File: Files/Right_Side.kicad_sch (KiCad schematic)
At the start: 77 parts, among them J4 USB_C_Receptacle, J5 Conn_01x03_Pin, J6 USB_C_Receptacle, U5 W25Q128JVS, U6 XC6206-3.3_SOT, U7 USBLC6-2SC6, U8 RP2040, Y2 Crystal_GND24

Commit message: placed companets and semi routed
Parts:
- C19, C20, C21, C22, C23, C24, C25, C27, C28, C29, C31, C32, C33, C34, C35, C36: footprint ScottoKeebs_Components:Capacitor_0603 -> Capacitor_SMD:C_0805_2012Metric_Pad1.18x1.45mm_HandSolder
- C26, C30: footprint ScottoKeebs_Components:Capacitor_0402 -> Capacitor_SMD:C_0805_2012Metric_Pad1.18x1.45mm_HandSolder
- R11, R12, R13, R14, R15, R16, R17, R18, R19, R20: footprint Resistor_SMD:R_0603_1608Metric -> Resistor_SMD:R_0805_2012Metric_Pad1.20x1.40mm_HandSolder
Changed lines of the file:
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@@
 			)
 		)
-		(property "Footprint" "ScottoKeebs_Components:Capacitor_0603"
+		(property "Footprint" "Capacitor_SMD:C_0805_2012Metric_Pad1.18x1.45mm_HandSolder"
 			(at 152.4 134.3152 0)
 			(effects
@@
 			)
 		)
-		(property "Footprint" "ScottoKeebs_Components:Capacitor_0402"
+		(property "Footprint" "Capacitor_SMD:C_0805_2012Metric_Pad1.18x1.45mm_HandSolder"
 			(at 191.4652 77.47 0)
 			(effects
@@
 			)
 		)
-		(property "Footprint" "ScottoKeebs_Components:Capacitor_0603"
+		(property "Footprint" "Capacitor_SMD:C_0805_2012Metric_Pad1.18x1.45mm_HandSolder"
 			(at 260.0452 62.23 0)
 			(effects
@@
 			)
 		)
-		(property "Footprint" "ScottoKeebs_Components:Capacitor_0603"
+		(property "Footprint" "Capacitor_SMD:C_0805_2012Metric_Pad1.18x1.45mm_HandSolder"
 			(at 118.11 108.2548 0)
 			(effects
@@
 			)
 		)
-		(property "Footprint" "ScottoKeebs_Components:Capacitor_0603"
+		(property "Footprint" "Capacitor_SMD:C_0805_2012Metric_Pad1.18x1.45mm_HandSolder"
 			(at 152.4 144.4752 0)
 			(effects
@@
 			)
 		)
-		(property "Footprint" "Resistor_SMD:R_0603_1608Metric"
+		(property "Footprint" "Resistor_SMD:R_0805_2012Metric_Pad1.20x1.40mm_HandSolder"
 			(at 190.5 96.012 90)
 			(effects
@@
 			)
 		)
-		(property "Footprint" "Resistor_SMD:R_0603_1608Metric"
+		(property "Footprint" "Resistor_SMD:R_0805_2012Metric_Pad1.20x1.40mm_HandSolder"
 			(at 92.71 187.198 90)
 			(effects
@@
 			)
 		)
-		(property "Footprint" "Resistor_SMD:R_0603_1608Metric"
+		(property "Footprint" "Resistor_SMD:R_0805_2012Metric_Pad1.20x1.40mm_HandSolder"
 			(at 216.662 209.55 90)
 			(effects
@@
 			)
 		)
-		(property "Footprint" "Resistor_SMD:R_0603_1608Metric"
+		(property "Footprint" "Resistor_SMD:R_0805_2012Metric_Pad1.20x1.40mm_HandSolder"
 			(at 186.69 145.288 90)
 			(effects
@@
 			)
 		)
-		(property "Footprint" "Resistor_SMD:R_0603_1608Metric"
+		(property "Footprint" "Resistor_SMD:R_0805_2012Metric_Pad1.20x1.40mm_HandSolder"
 			(at 81.28 116.078 90)
 			(effects
@@
 			)
 		)
-		(property "Footprint" "Resistor_SMD:R_0603_1608Metric"
+		(property "Footprint" "Resistor_SMD:R_0805_2012Metric_Pad1.20x1.40mm_HandSolder"
 			(at 92.71 189.738 90)
 			(effects
@@
 			)
 		)
-		(property "Footprint" "ScottoKeebs_Components:Capacitor_0603"
+		(property "Footprint" "Capacitor_SMD:C_0805_2012Metric_Pad1.18x1.45mm_HandSolder"
 			(at 246.0752 43.18 0)
 			(effects
@@
 			)
 		)
-		(property "Footprint" "ScottoKeebs_Components:Capacitor_0603"
+		(property "Footprint" "Capacitor_SMD:C_0805_2012Metric_Pad1.18x1.45mm_HandSolder"
 			(at 191.4652 62.23 0)
 			(effects
@@
 			)
 		)
-		(property "Footprint" "ScottoKeebs_Components:Capacitor_0603"
+		(property "Footprint" "Capacitor_SMD:C_0805_2012Metric_Pad1.18x1.45mm_HandSolder"
 			(at 296.8752 62.23 0)
 			(effects
@@
 			)
 		)
-		(property "Footprint" "Resistor_SMD:R_0603_1608Metric"
+		(property "Footprint" "Resistor_SMD:R_0805_2012Metric_Pad1.20x1.40mm_HandSolder"
 			(at 186.182 209.55 90)
 			(effects
@@
 			)
 		)
-		(property "Footprint" "ScottoKeebs_Components:Capacitor_0603"
+		(property "Footprint" "Capacitor_SMD:C_0805_2012Metric_Pad1.18x1.45mm_HandSolder"
 			(at 323.5452 62.23 0)
 			(effects
@@
 			)
 		)
-		(property "Footprint" "ScottoKeebs_Components:Capacitor_0603"
+		(property "Footprint" "Capacitor_SMD:C_0805_2012Metric_Pad1.18x1.45mm_HandSolder"
 			(at 284.1752 62.23 0)
 			(effects
@@
 			)
 		)
-		(property "Footprint" "ScottoKeebs_Components:Capacitor_0603"
+		(property "Footprint" "Capacitor_SMD:C_0805_2012Metric_Pad1.18x1.45mm_HandSolder"
 			(at 110.1852 187.96 0)
 			(effects
@@
 			)
 		)
-		(property "Footprint" "Resistor_SMD:R_0603_1608Metric"
+		(property "Footprint" "Resistor_SMD:R_0805_2012Metric_Pad1.20x1.40mm_HandSolder"
 			(at 190.5 97.028 90)
 			(effects
@@
 			)
 		)
-		(property "Footprint" "ScottoKeebs_Components:Capacitor_0603"
+		(property "Footprint" "Capacitor_SMD:C_0805_2012Metric_Pad1.18x1.45mm_HandSolder"
 			(at 247.3452 62.23 0)
 			(effects
@@
 			)
 		)
-		(property "Footprint" "ScottoKeebs_Components:Capacitor_0603"
+		(property "Footprint" "Capacitor_SMD:C_0805_2012Metric_Pad1.18x1.45mm_HandSolder"
 			(at 202.8952 62.23 0)
 			(effects
@@
 			)
 		)
-		(property "Footprint" "ScottoKeebs_Components:Capacitor_0603"
+		(property "Footprint" "Capacitor_SMD:C_0805_2012Metric_Pad1.18x1.45mm_HandSolder"
 			(at 89.2048 58.42 0)
 			(effects
@@
 			)
 		)
-		(property "Footprint" "ScottoKeebs_Components:Capacitor_0603"
+		(property "Footprint" "Capacitor_SMD:C_0805_2012Metric_Pad1.18x1.45mm_HandSolder"
 			(at 272.7452 62.23 0)
 			(effects
@@
 			)
 		)
-		(property "Footprint" "Resistor_SMD:R_0603_1608Metric"
+		(property "Footprint" "Resistor_SMD:R_0805_2012Metric_Pad1.20x1.40mm_HandSolder"
 			(at 82.042 52.07 90)
 			(effects
@@
 			)
 		)
-		(property "Footprint" "ScottoKeebs_Components:Capacitor_0402"
+		(property "Footprint" "Capacitor_SMD:C_0805_2012Metric_Pad1.18x1.45mm_HandSolder"
 			(at 247.3452 77.47 0)
 			(effects
@@
 			)
 		)
-		(property "Footprint" "Resistor_SMD:R_0603_1608Metric"
+		(property "Footprint" "Resistor_SMD:R_0805_2012Metric_Pad1.20x1.40mm_HandSolder"
 			(at 91.948 113.03 90)
 			(effects
@@
 			)
 		)
-		(property "Footprint" "ScottoKeebs_Components:Capacitor_0603"
+		(property "Footprint" "Capacitor_SMD:C_0805_2012Metric_Pad1.18x1.45mm_HandSolder"
 			(at 309.5752 62.23 0)
 			(effects
@@
 			)
 		)
-		(property "Footprint" "ScottoKeebs_Components:Capacitor_0603"
+		(property "Footprint" "Capacitor_SMD:C_0805_2012Metric_Pad1.18x1.45mm_HandSolder"
 			(at 143.2052 187.96 0)
 			(effects

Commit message: added 5v pads
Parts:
- C19, C20, C21, C22, C23, C24, C25, C26, C27, C28, C29, C30, C31, C32, C33, C34, C35, C36: footprint Capacitor_SMD:C_0805_2012Metric_Pad1.18x1.45mm_HandSolder -> Capacitor_SMD:C_0805_2012Metric
- R11, R12, R13, R14, R15, R16, R17, R18, R19, R20: footprint Resistor_SMD:R_0805_2012Metric_Pad1.20x1.40mm_HandSolder -> Resistor_SMD:R_0805_2012Metric
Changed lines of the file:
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@@
 			)
 		)
-		(property "Footprint" "Capacitor_SMD:C_0805_2012Metric_Pad1.18x1.45mm_HandSolder"
+		(property "Footprint" "Capacitor_SMD:C_0805_2012Metric"
 			(at 152.4 134.3152 0)
 			(effects
@@
 			)
 		)
-		(property "Footprint" "Capacitor_SMD:C_0805_2012Metric_Pad1.18x1.45mm_HandSolder"
+		(property "Footprint" "Capacitor_SMD:C_0805_2012Metric"
 			(at 191.4652 77.47 0)
 			(effects
@@
 			)
 		)
-		(property "Footprint" "Capacitor_SMD:C_0805_2012Metric_Pad1.18x1.45mm_HandSolder"
+		(property "Footprint" "Capacitor_SMD:C_0805_2012Metric"
 			(at 260.0452 62.23 0)
 			(effects
@@
 			)
 		)
-		(property "Footprint" "Capacitor_SMD:C_0805_2012Metric_Pad1.18x1.45mm_HandSolder"
+		(property "Footprint" "Capacitor_SMD:C_0805_2012Metric"
 			(at 118.11 108.2548 0)
 			(effects
@@
 			)
 		)
-		(property "Footprint" "Capacitor_SMD:C_0805_2012Metric_Pad1.18x1.45mm_HandSolder"
+		(property "Footprint" "Capacitor_SMD:C_0805_2012Metric"
 			(at 152.4 144.4752 0)
 			(effects
@@
 			)
 		)
-		(property "Footprint" "Resistor_SMD:R_0805_2012Metric_Pad1.20x1.40mm_HandSolder"
+		(property "Footprint" "Resistor_SMD:R_0805_2012Metric"
 			(at 190.5 96.012 90)
 			(effects
@@
 			)
 		)
-		(property "Footprint" "Resistor_SMD:R_0805_2012Metric_Pad1.20x1.40mm_HandSolder"
+		(property "Footprint" "Resistor_SMD:R_0805_2012Metric"
 			(at 92.71 187.198 90)
 			(effects
@@
 			)
 		)
-		(property "Footprint" "Resistor_SMD:R_0805_2012Metric_Pad1.20x1.40mm_HandSolder"
+		(property "Footprint" "Resistor_SMD:R_0805_2012Metric"
 			(at 216.662 209.55 90)
 			(effects
@@
 			)
 		)
-		(property "Footprint" "Resistor_SMD:R_0805_2012Metric_Pad1.20x1.40mm_HandSolder"
+		(property "Footprint" "Resistor_SMD:R_0805_2012Metric"
 			(at 186.69 145.288 90)
 			(effects
@@
 			)
 		)
-		(property "Footprint" "Resistor_SMD:R_0805_2012Metric_Pad1.20x1.40mm_HandSolder"
+		(property "Footprint" "Resistor_SMD:R_0805_2012Metric"
 			(at 81.28 116.078 90)
 			(effects
@@
 			)
 		)
-		(property "Footprint" "Resistor_SMD:R_0805_2012Metric_Pad1.20x1.40mm_HandSolder"
+		(property "Footprint" "Resistor_SMD:R_0805_2012Metric"
 			(at 92.71 189.738 90)
 			(effects
@@
 			)
 		)
-		(property "Footprint" "Capacitor_SMD:C_0805_2012Metric_Pad1.18x1.45mm_HandSolder"
+		(property "Footprint" "Capacitor_SMD:C_0805_2012Metric"
 			(at 246.0752 43.18 0)
 			(effects
@@
 			)
 		)
-		(property "Footprint" "Capacitor_SMD:C_0805_2012Metric_Pad1.18x1.45mm_HandSolder"
+		(property "Footprint" "Capacitor_SMD:C_0805_2012Metric"
 			(at 191.4652 62.23 0)
 			(effects
@@
 			)
 		)
-		(property "Footprint" "Capacitor_SMD:C_0805_2012Metric_Pad1.18x1.45mm_HandSolder"
+		(property "Footprint" "Capacitor_SMD:C_0805_2012Metric"
 			(at 296.8752 62.23 0)
 			(effects
@@
 			)
 		)
-		(property "Footprint" "Resistor_SMD:R_0805_2012Metric_Pad1.20x1.40mm_HandSolder"
+		(property "Footprint" "Resistor_SMD:R_0805_2012Metric"
 			(at 186.182 209.55 90)
 			(effects
@@
 			)
 		)
-		(property "Footprint" "Capacitor_SMD:C_0805_2012Metric_Pad1.18x1.45mm_HandSolder"
+		(property "Footprint" "Capacitor_SMD:C_0805_2012Metric"
 			(at 323.5452 62.23 0)
 			(effects
@@
 			)
 		)
-		(property "Footprint" "Capacitor_SMD:C_0805_2012Metric_Pad1.18x1.45mm_HandSolder"
+		(property "Footprint" "Capacitor_SMD:C_0805_2012Metric"
 			(at 284.1752 62.23 0)
 			(effects
@@
 			)
 		)
-		(property "Footprint" "Capacitor_SMD:C_0805_2012Metric_Pad1.18x1.45mm_HandSolder"
+		(property "Footprint" "Capacitor_SMD:C_0805_2012Metric"
 			(at 110.1852 187.96 0)
 			(effects
@@
 			)
 		)
-		(property "Footprint" "Resistor_SMD:R_0805_2012Metric_Pad1.20x1.40mm_HandSolder"
+		(property "Footprint" "Resistor_SMD:R_0805_2012Metric"
 			(at 190.5 97.028 90)
 			(effects
@@
 			)
 		)
-		(property "Footprint" "Capacitor_SMD:C_0805_2012Metric_Pad1.18x1.45mm_HandSolder"
+		(property "Footprint" "Capacitor_SMD:C_0805_2012Metric"
 			(at 247.3452 62.23 0)
 			(effects
@@
 			)
 		)
-		(property "Footprint" "Capacitor_SMD:C_0805_2012Metric_Pad1.18x1.45mm_HandSolder"
+		(property "Footprint" "Capacitor_SMD:C_0805_2012Metric"
 			(at 202.8952 62.23 0)
 			(effects
@@
 			)
 		)
-		(property "Footprint" "Capacitor_SMD:C_0805_2012Metric_Pad1.18x1.45mm_HandSolder"
+		(property "Footprint" "Capacitor_SMD:C_0805_2012Metric"
 			(at 89.2048 58.42 0)
 			(effects
@@
 			)
 		)
-		(property "Footprint" "Capacitor_SMD:C_0805_2012Metric_Pad1.18x1.45mm_HandSolder"
+		(property "Footprint" "Capacitor_SMD:C_0805_2012Metric"
 			(at 272.7452 62.23 0)
 			(effects
@@
 			)
 		)
-		(property "Footprint" "Resistor_SMD:R_0805_2012Metric_Pad1.20x1.40mm_HandSolder"
+		(property "Footprint" "Resistor_SMD:R_0805_2012Metric"
 			(at 82.042 52.07 90)
 			(effects
@@
 			)
 		)
-		(property "Footprint" "Capacitor_SMD:C_0805_2012Metric_Pad1.18x1.45mm_HandSolder"
+		(property "Footprint" "Capacitor_SMD:C_0805_2012Metric"
 			(at 247.3452 77.47 0)
 			(effects
@@
 			)
 		)
-		(property "Footprint" "Resistor_SMD:R_0805_2012Metric_Pad1.20x1.40mm_HandSolder"
+		(property "Footprint" "Resistor_SMD:R_0805_2012Metric"
 			(at 91.948 113.03 90)
 			(effects
@@
 			)
 		)
-		(property "Footprint" "Capacitor_SMD:C_0805_2012Metric_Pad1.18x1.45mm_HandSolder"
+		(property "Footprint" "Capacitor_SMD:C_0805_2012Metric"
 			(at 309.5752 62.23 0)
 			(effects
@@
 			)
 		)
-		(property "Footprint" "Capacitor_SMD:C_0805_2012Metric_Pad1.18x1.45mm_HandSolder"
+		(property "Footprint" "Capacitor_SMD:C_0805_2012Metric"
 			(at 143.2052 187.96 0)
 			(effects

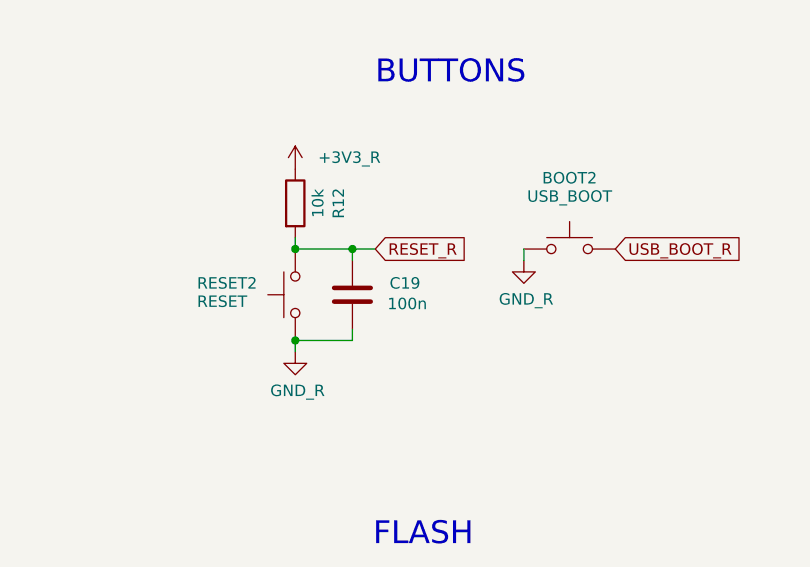
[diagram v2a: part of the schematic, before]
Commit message: converted to 4 layer board
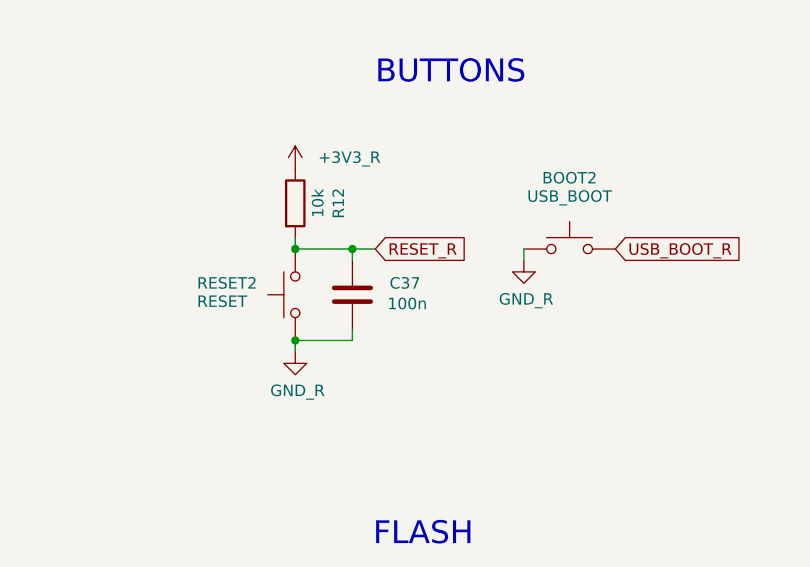
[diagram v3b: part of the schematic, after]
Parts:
- C20, C21, C22, C23, C24, C25, C26, C27, C28, C29, C30, C31, C32, C33, C34, C35, C36: footprint Capacitor_SMD:C_0805_2012Metric -> Capacitor_SMD:C_0603_1608Metric
- C37: renamed from C19; footprint Capacitor_SMD:C_0805_2012Metric -> Capacitor_SMD:C_0603_1608Metric
- R11, R12, R13, R14, R15, R16, R17, R18, R19, R20: footprint Resistor_SMD:R_0805_2012Metric -> Resistor_SMD:R_0603_1608Metric
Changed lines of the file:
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@@
 			)
 		)
-		(property "Footprint" "Capacitor_SMD:C_0805_2012Metric"
+		(property "Footprint" "Capacitor_SMD:C_0603_1608Metric"
 			(at 152.4 134.3152 0)
 			(effects
@@
 			)
 		)
-		(property "Footprint" "Capacitor_SMD:C_0805_2012Metric"
+		(property "Footprint" "Capacitor_SMD:C_0603_1608Metric"
 			(at 191.4652 77.47 0)
 			(effects
@@
 			)
 		)
-		(property "Footprint" "Capacitor_SMD:C_0805_2012Metric"
+		(property "Footprint" "Capacitor_SMD:C_0603_1608Metric"
 			(at 260.0452 62.23 0)
 			(effects
@@
 			)
 		)
-		(property "Footprint" "Capacitor_SMD:C_0805_2012Metric"
+		(property "Footprint" "Capacitor_SMD:C_0603_1608Metric"
 			(at 118.11 108.2548 0)
 			(effects
@@
 			)
 		)
-		(property "Footprint" "Capacitor_SMD:C_0805_2012Metric"
+		(property "Footprint" "Capacitor_SMD:C_0603_1608Metric"
 			(at 152.4 144.4752 0)
 			(effects
@@
 			)
 		)
-		(property "Footprint" "Resistor_SMD:R_0805_2012Metric"
+		(property "Footprint" "Resistor_SMD:R_0603_1608Metric"
 			(at 190.5 96.012 90)
 			(effects
@@
 			)
 		)
-		(property "Footprint" "Resistor_SMD:R_0805_2012Metric"
+		(property "Footprint" "Resistor_SMD:R_0603_1608Metric"
 			(at 92.71 187.198 90)
 			(effects
@@
 			)
 		)
-		(property "Footprint" "Resistor_SMD:R_0805_2012Metric"
+		(property "Footprint" "Resistor_SMD:R_0603_1608Metric"
 			(at 216.662 209.55 90)
 			(effects
@@
 			)
 		)
-		(property "Footprint" "Resistor_SMD:R_0805_2012Metric"
+		(property "Footprint" "Resistor_SMD:R_0603_1608Metric"
 			(at 186.69 145.288 90)
 			(effects
@@
 			)
 		)
-		(property "Footprint" "Resistor_SMD:R_0805_2012Metric"
+		(property "Footprint" "Resistor_SMD:R_0603_1608Metric"
 			(at 81.28 116.078 90)
 			(effects
@@
 			)
 		)
-		(property "Footprint" "Resistor_SMD:R_0805_2012Metric"
+		(property "Footprint" "Resistor_SMD:R_0603_1608Metric"
 			(at 92.71 189.738 90)
 			(effects
@@
 			)
 		)
-		(property "Footprint" "Capacitor_SMD:C_0805_2012Metric"
+		(property "Footprint" "Capacitor_SMD:C_0603_1608Metric"
 			(at 246.0752 43.18 0)
 			(effects
@@
 			)
 		)
-		(property "Footprint" "Capacitor_SMD:C_0805_2012Metric"
+		(property "Footprint" "Capacitor_SMD:C_0603_1608Metric"
 			(at 191.4652 62.23 0)
 			(effects
@@
 			)
 		)
-		(property "Footprint" "Capacitor_SMD:C_0805_2012Metric"
+		(property "Footprint" "Capacitor_SMD:C_0603_1608Metric"
 			(at 296.8752 62.23 0)
 			(effects
@@
 			)
 		)
-		(property "Footprint" "Resistor_SMD:R_0805_2012Metric"
+		(property "Footprint" "Resistor_SMD:R_0603_1608Metric"
 			(at 186.182 209.55 90)
 			(effects
@@
 			)
 		)
-		(property "Footprint" "Capacitor_SMD:C_0805_2012Metric"
+		(property "Footprint" "Capacitor_SMD:C_0603_1608Metric"
 			(at 323.5452 62.23 0)
 			(effects
@@
 			)
 		)
-		(property "Footprint" "Capacitor_SMD:C_0805_2012Metric"
+		(property "Footprint" "Capacitor_SMD:C_0603_1608Metric"
 			(at 284.1752 62.23 0)
 			(effects
@@
 			)
 		)
-		(property "Footprint" "Capacitor_SMD:C_0805_2012Metric"
+		(property "Footprint" "Capacitor_SMD:C_0603_1608Metric"
 			(at 110.1852 187.96 0)
 			(effects
@@
 			)
 		)
-		(property "Footprint" "Resistor_SMD:R_0805_2012Metric"
+		(property "Footprint" "Resistor_SMD:R_0603_1608Metric"
 			(at 190.5 97.028 90)
 			(effects
@@
 			)
 		)
-		(property "Footprint" "Capacitor_SMD:C_0805_2012Metric"
+		(property "Footprint" "Capacitor_SMD:C_0603_1608Metric"
 			(at 247.3452 62.23 0)
 			(effects
@@
 			)
 		)
-		(property "Footprint" "Capacitor_SMD:C_0805_2012Metric"
+		(property "Footprint" "Capacitor_SMD:C_0603_1608Metric"
 			(at 202.8952 62.23 0)
 			(effects
@@
 		(on_board yes)
 		(dnp no)
-		(property "Reference" "C19"
+		(property "Reference" "C37"
 			(at 96.012 60.96 0)
 			(effects
@@
 			)
 		)
-		(property "Footprint" "Capacitor_SMD:C_0805_2012Metric"
+		(property "Footprint" "Capacitor_SMD:C_0603_1608Metric"
 			(at 89.2048 58.42 0)
 			(effects
@@
 			(project "CustomKB2040"
 				(path "/1dc59942-63a2-41f5-a9fb-7502b7672a2f/509c21e9-3c87-4ca7-a30c-cd35896bf815"
-					(reference "C19")
+					(reference "C37")
 					(unit 1)
 				)
@@
 			)
 		)
-		(property "Footprint" "Capacitor_SMD:C_0805_2012Metric"
+		(property "Footprint" "Capacitor_SMD:C_0603_1608Metric"
 			(at 272.7452 62.23 0)
 			(effects
@@
 			)
 		)
-		(property "Footprint" "Resistor_SMD:R_0805_2012Metric"
+		(property "Footprint" "Resistor_SMD:R_0603_1608Metric"
 			(at 82.042 52.07 90)
 			(effects
@@
 			)
 		)
-		(property "Footprint" "Capacitor_SMD:C_0805_2012Metric"
+		(property "Footprint" "Capacitor_SMD:C_0603_1608Metric"
 			(at 247.3452 77.47 0)
 			(effects
@@
 			)
 		)
-		(property "Footprint" "Resistor_SMD:R_0805_2012Metric"
+		(property "Footprint" "Resistor_SMD:R_0603_1608Metric"
 			(at 91.948 113.03 90)
 			(effects
@@
 			)
 		)
-		(property "Footprint" "Capacitor_SMD:C_0805_2012Metric"
+		(property "Footprint" "Capacitor_SMD:C_0603_1608Metric"
 			(at 309.5752 62.23 0)
 			(effects
@@
 			)
 		)
-		(property "Footprint" "Capacitor_SMD:C_0805_2012Metric"
+		(property "Footprint" "Capacitor_SMD:C_0603_1608Metric"
 			(at 143.2052 187.96 0)
 			(effects

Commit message: Finished left side
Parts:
- renumbered D3 to D41, D4 to D42
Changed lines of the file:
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@@
 		(dnp no)
 		(fields_autoplaced yes)
-		(property "Reference" "D3"
+		(property "Reference" "D41"
 			(at 191.77 217.4874 90)
 			(effects
@@
 			(project "CustomKB2040"
 				(path "/1dc59942-63a2-41f5-a9fb-7502b7672a2f/509c21e9-3c87-4ca7-a30c-cd35896bf815"
-					(reference "D3")
+					(reference "D41")
 					(unit 1)
 				)
@@
 		(dnp no)
 		(fields_autoplaced yes)
-		(property "Reference" "D4"
+		(property "Reference" "D42"
 			(at 222.25 217.4874 90)
 			(effects
@@
 			(project "CustomKB2040"
 				(path "/1dc59942-63a2-41f5-a9fb-7502b7672a2f/509c21e9-3c87-4ca7-a30c-cd35896bf815"
-					(reference "D4")
+					(reference "D42")
 					(unit 1)
 				)
